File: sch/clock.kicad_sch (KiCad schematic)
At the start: 7 parts, among them U2 74AHC74

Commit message: Clearances
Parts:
- R30: value 10K -> (none)
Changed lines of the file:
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@@
       (effects (font (size 1.27 1.27)) (justify right))
     )
-    (property "Value" "10K" (id 1) (at 57.785 88.265 0)
+    (property "Value" "" (id 1) (at 57.785 88.265 0)
       (effects (font (size 1.27 1.27)) (justify right))
     )

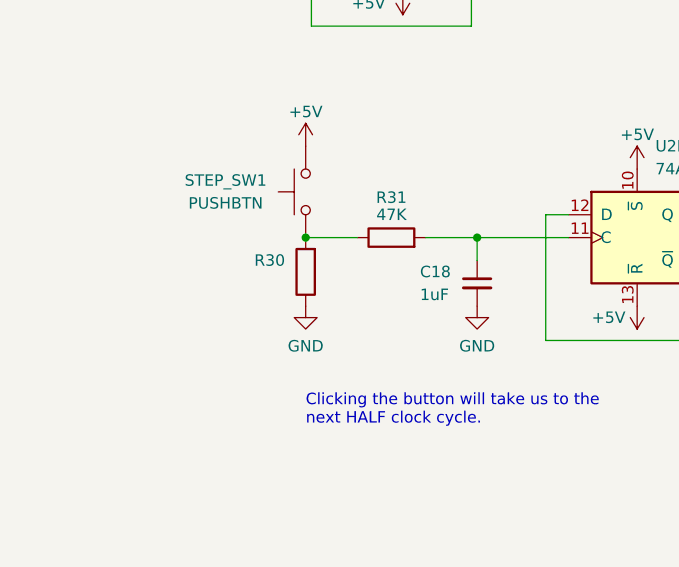
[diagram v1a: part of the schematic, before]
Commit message: Huge mistake CPU fp
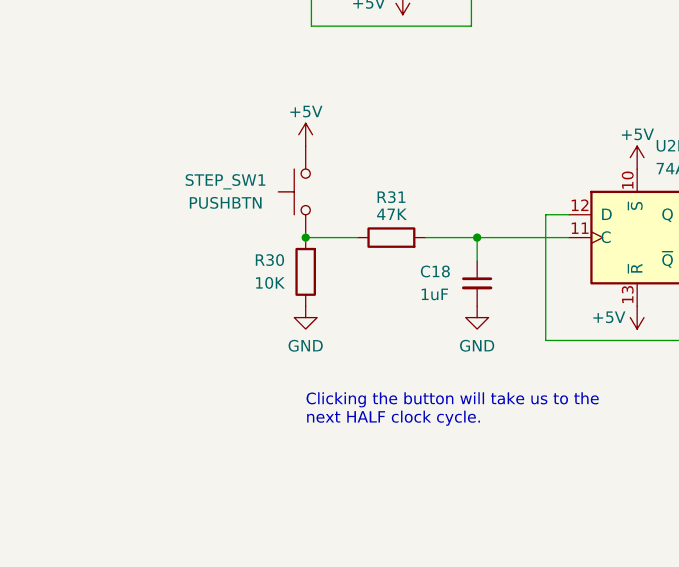
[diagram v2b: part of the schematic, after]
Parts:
- R30: value (none) -> 10K
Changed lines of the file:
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@@
       (effects (font (size 1.27 1.27)) (justify right))
     )
-    (property "Value" "" (id 1) (at 57.785 88.265 0)
+    (property "Value" "10K" (id 1) (at 57.785 88.265 0)
       (effects (font (size 1.27 1.27)) (justify right))
     )
